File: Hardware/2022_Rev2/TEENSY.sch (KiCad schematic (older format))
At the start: 8 parts

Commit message: back to the teensy :alien:
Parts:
- removed U? (x8): TM4C129E_Launchpad, symbol MRDT_Shields:TM4C129E_Launchpad
- added U?: Teensy4.1_DEV-16771-MRDT_Shields, MODULE_DEV-16771, symbol 2022_Rev2-rescue:Teensy4.1_DEV-16771-MRDT_Shields
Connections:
- no-connect marks 0 -> 42
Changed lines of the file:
@@
 $Descr A4 11693 8268
 encoding utf-8
-Sheet 4 5
+Sheet 5 6
 Title ""
 Date ""
@@
 L power:GND #PWR?
 U 1 1 62120694
-P 6450 5600
-F 0 "#PWR?" H 6450 5350 50  0001 C CNN
-F 1 "GND" H 6455 5427 50  0000 C CNN
-F 2 "" H 6450 5600 50  0001 C CNN
-F 3 "" H 6450 5600 50  0001 C CNN
-	1    6450 5600
+P 6000 6100
+F 0 "#PWR?" H 6000 5850 50  0001 C CNN
+F 1 "GND" H 6005 5927 50  0000 C CNN
+F 2 "" H 6000 6100 50  0001 C CNN
+F 3 "" H 6000 6100 50  0001 C CNN
+	1    6000 6100
 	1    0    0    -1
 $EndComp
 Wire Wire Line
-	6250 5400 6450 5400
+	5800 5900 6000 5900
 Wire Wire Line
-	6450 5400 6450 5500
+	6000 5900 6000 6000
 Wire Wire Line
-	6250 5500 6450 5500
-Connection ~ 6450 5500
+	5800 6000 6000 6000
+Connection ~ 6000 6000
 Wire Wire Line
-	6450 5500 6450 5600
+	6000 6000 6000 6100
 $Comp
 L power:+3.3V #PWR?
 U 1 1 6220549B
-P 6550 1500
-F 0 "#PWR?" H 6550 1350 50  0001 C CNN
-F 1 "+3.3V" H 6565 1673 50  0000 C CNN
-F 2 "" H 6550 1500 50  0001 C CNN
-F 3 "" H 6550 1500 50  0001 C CNN
-	1    6550 1500
+P 6000 2100
+F 0 "#PWR?" H 6000 1950 50  0001 C CNN
+F 1 "+3.3V" H 6015 2273 50  0000 C CNN
+F 2 "" H 6000 2100 50  0001 C CNN
+F 3 "" H 6000 2100 50  0001 C CNN
+	1    6000 2100
 	1    0    0    -1
 $EndComp
 Wire Wire Line
-	6350 1700 6550 1700
+	5800 2300 6000 2300
 Wire Wire Line
-	6550 1700 6550 1500
-Text HLabel 3750 5150 0    50   Input ~ 0
+	6000 2300 6000 2100
+Text HLabel 4100 5400 0    50   Input ~ 0
 Current_Sense_BlackBox
-Text HLabel 3750 5050 0    50   Input ~ 0
+Text HLabel 4100 5300 0    50   Input ~ 0
 Current_Sense_Multimedia
-Text HLabel 3750 4950 0    50   Input ~ 0
+Text HLabel 4100 5200 0    50   Input ~ 0
 Current_Sense_Drive
-Text HLabel 3750 4850 0    50   Input ~ 0
+Text HLabel 4100 5100 0    50   Input ~ 0
 Current_Sense_Nav
-Text HLabel 3750 4750 0    50   Input ~ 0
+Text HLabel 4100 5000 0    50   Input ~ 0
 Current_Sense_Gimbal
-Text HLabel 3750 4650 0    50   Input ~ 0
+Text HLabel 4100 4900 0    50   Input ~ 0
 Current_Sense_Spare
 Wire Wire Line
-	3750 4650 3850 4650
+	4100 4900 4200 4900
 Wire Wire Line
-	3850 4750 3750 4750
+	4200 5000 4100 5000
 Wire Wire Line
-	3750 4850 3850 4850
+	4100 5100 4200 5100
 Wire Wire Line
-	3850 4950 3750 4950
+	4200 5200 4100 5200
 Wire Wire Line
-	3750 5050 3850 5050
+	4100 5300 4200 5300
 Wire Wire Line
-	3850 5150 3750 5150
-Text HLabel 3750 3050 0    50   Output ~ 0
+	4200 5400 4100 5400
+Text HLabel 4100 3300 0    50   Output ~ 0
 Driver_BlackBox
-Text HLabel 3750 3150 0    50   Output ~ 0
+Text HLabel 4100 3400 0    50   Output ~ 0
 Driver_Multimedia
-Text HLabel 3750 3250 0    50   Output ~ 0
+Text HLabel 4100 3500 0    50   Output ~ 0
 Driver_Drive
-Text HLabel 3750 3350 0    50   Output ~ 0
+Text HLabel 4100 3600 0    50   Output ~ 0
 Driver_Nav
-Text HLabel 3750 3450 0    50   Output ~ 0
+Text HLabel 4100 3700 0    50   Output ~ 0
 Driver_Gimbal
-Text HLabel 3750 3550 0    50   Output ~ 0
+Text HLabel 4100 3800 0    50   Output ~ 0
 Driver_Spare
 Wire Wire Line
-	3750 3050 3850 3050
+	4100 3300 4200 3300
 Wire Wire Line
-	3850 3150 3750 3150
+	4200 3400 4100 3400
 Wire Wire Line
-	3750 3250 3850 3250
+	4100 3500 4200 3500
 Wire Wire Line
-	3850 3350 3750 3350
+	4200 3600 4100 3600
 Wire Wire Line
-	3750 3450 3850 3450
+	4100 3700 4200 3700
 Wire Wire Line
-	3850 3550 3750 3550
+	4200 3800 4100 3800
 $Comp
-L MRDT_Shields:TM4C129E_Launchpad U?
-U 1 1 622A6302
-P 5000 3300
-F 0 "U?" H 5301 3898 60  0000 L CNN
-F 1 "TM4C129E_Launchpad" H 5301 3792 60  0000 L CNN
-F 2 "" H 5000 3300 60  0001 C CNN
-F 3 "" H 5000 3300 60  0001 C CNN
-	1    5000 3300
+L 2022_Rev2-rescue:Teensy4.1_DEV-16771-MRDT_Shields U?
+U 1 1 62325DE4
+P 5000 4100
+F 0 "U?" H 5000 6267 50  0000 C CNN
+F 1 "Teensy4.1_DEV-16771-MRDT_Shields" H 5000 6176 50  0000 C CNN
+F 2 "MODULE_DEV-16771" H 7100 3800 50  0001 L BNN
+F 3 "" H 5000 4100 50  0001 L BNN
+F 4 "Manufacturer recommendations" H 7100 3550 50  0001 L BNN "STANDARD"
+F 5 "4.07mm" H 7350 3350 50  0001 L BNN "MAXIMUM_PACKAGE_HEIGHT"
+F 6 "SparkFun Electronics" H 7300 3200 50  0001 L BNN "MANUFACTURER"
+F 7 "4.1" H 4700 1900 50  0001 L BNN "PARTREV"
+	1    5000 4100
 	1    0    0    -1
 $EndComp
-$Comp
-L MRDT_Shields:TM4C129E_Launchpad U?
-U 2 1 622A854E
-P 6700 3250
-F 0 "U?" H 6731 4527 60  0000 C CNN
-F 1 "TM4C129E_Launchpad" H 6731 4421 60  0000 C CNN
-F 2 "" H 6700 3250 60  0001 C CNN
-F 3 "" H 6700 3250 60  0001 C CNN
-	2    6700 3250
-	-1   0    0    -1
-$EndComp
-$Comp
-L MRDT_Shields:TM4C129E_Launchpad U?
-U 3 1 622AA5F6
-P 7950 3250
-F 0 "U?" H 8255 3848 60  0000 L CNN
-F 1 "TM4C129E_Launchpad" H 8255 3742 60  0000 L CNN
-F 2 "" H 7950 3250 60  0001 C CNN
-F 3 "" H 7950 3250 60  0001 C CNN
-	3    7950 3250
-	1    0    0    -1
-$EndComp
-$Comp
-L MRDT_Shields:TM4C129E_Launchpad U?
-U 4 1 622AE2B5
-P 9800 3200
-F 0 "U?" H 9831 4477 60  0000 C CNN
-F 1 "TM4C129E_Launchpad" H 9831 4371 60  0000 C CNN
-F 2 "" H 9800 3200 60  0001 C CNN
-F 3 "" H 9800 3200 60  0001 C CNN
-	4    9800 3200
-	-1   0    0    -1
-$EndComp
-$Comp
-L MRDT_Shields:TM4C129E_Launchpad U?
-U 5 1 622B0F3D
-P 5000 4650
-F 0 "U?" H 5301 5248 60  0000 L CNN
-F 1 "TM4C129E_Launchpad" H 5301 5142 60  0000 L CNN
-F 2 "" H 5000 4650 60  0001 C CNN
-F 3 "" H 5000 4650 60  0001 C CNN
-	5    5000 4650
-	1    0    0    -1
-$EndComp
-$Comp
-L MRDT_Shields:TM4C129E_Launchpad U?
-U 6 1 622B4CAE
-P 6700 4700
-F 0 "U?" H 6731 5977 60  0000 C CNN
-F 1 "TM4C129E_Launchpad" H 6731 5871 60  0000 C CNN
-F 2 "" H 6700 4700 60  0001 C CNN
-F 3 "" H 6700 4700 60  0001 C CNN
-	6    6700 4700
-	-1   0    0    -1
-$EndComp
-$Comp
-L MRDT_Shields:TM4C129E_Launchpad U?
-U 7 1 622B6EBF
-P 7950 4750
-F 0 "U?" H 8255 5348 60  0000 L CNN
-F 1 "TM4C129E_Launchpad" H 8255 5242 60  0000 L CNN
-F 2 "" H 7950 4750 60  0001 C CNN
-F 3 "" H 7950 4750 60  0001 C CNN
-	7    7950 4750
-	1    0    0    -1
-$EndComp
-$Comp
-L MRDT_Shields:TM4C129E_Launchpad U?
-U 8 1 622B9460
-P 9750 4750
-F 0 "U?" H 9781 6027 60  0000 C CNN
-F 1 "TM4C129E_Launchpad" H 9781 5921 60  0000 C CNN
-F 2 "" H 9750 4750 60  0001 C CNN
-F 3 "" H 9750 4750 60  0001 C CNN
-	8    9750 4750
-	-1   0    0    -1
-$EndComp
+NoConn ~ 4200 2700
+NoConn ~ 4200 2800
+NoConn ~ 4200 3000
+NoConn ~ 4200 3100
+NoConn ~ 4200 3900
+NoConn ~ 4200 4000
+NoConn ~ 4200 4100
+NoConn ~ 4200 4200
+NoConn ~ 4200 4400
+NoConn ~ 4200 4500
+NoConn ~ 4200 4600
+NoConn ~ 4200 4700
+NoConn ~ 4200 5500
+NoConn ~ 4200 5600
+NoConn ~ 4200 5700
+NoConn ~ 5800 5700
+NoConn ~ 5800 5600
+NoConn ~ 5800 5500
+NoConn ~ 5800 5400
+NoConn ~ 5800 5300
+NoConn ~ 5800 5200
+NoConn ~ 5800 5100
+NoConn ~ 5800 5000
+NoConn ~ 5800 4900
+NoConn ~ 5800 4600
+NoConn ~ 5800 4500
+NoConn ~ 5800 4300
+NoConn ~ 5800 4200
+NoConn ~ 5800 4100
+NoConn ~ 5800 3900
+NoConn ~ 5800 3800
+NoConn ~ 5800 3700
+NoConn ~ 5800 3600
+NoConn ~ 5800 3400
+NoConn ~ 5800 3300
+NoConn ~ 5800 3100
+NoConn ~ 5800 3000
+NoConn ~ 5800 2900
+NoConn ~ 5800 2800
+NoConn ~ 5800 2700
+NoConn ~ 5800 2500
+NoConn ~ 5800 2400
 $EndSCHEMATC

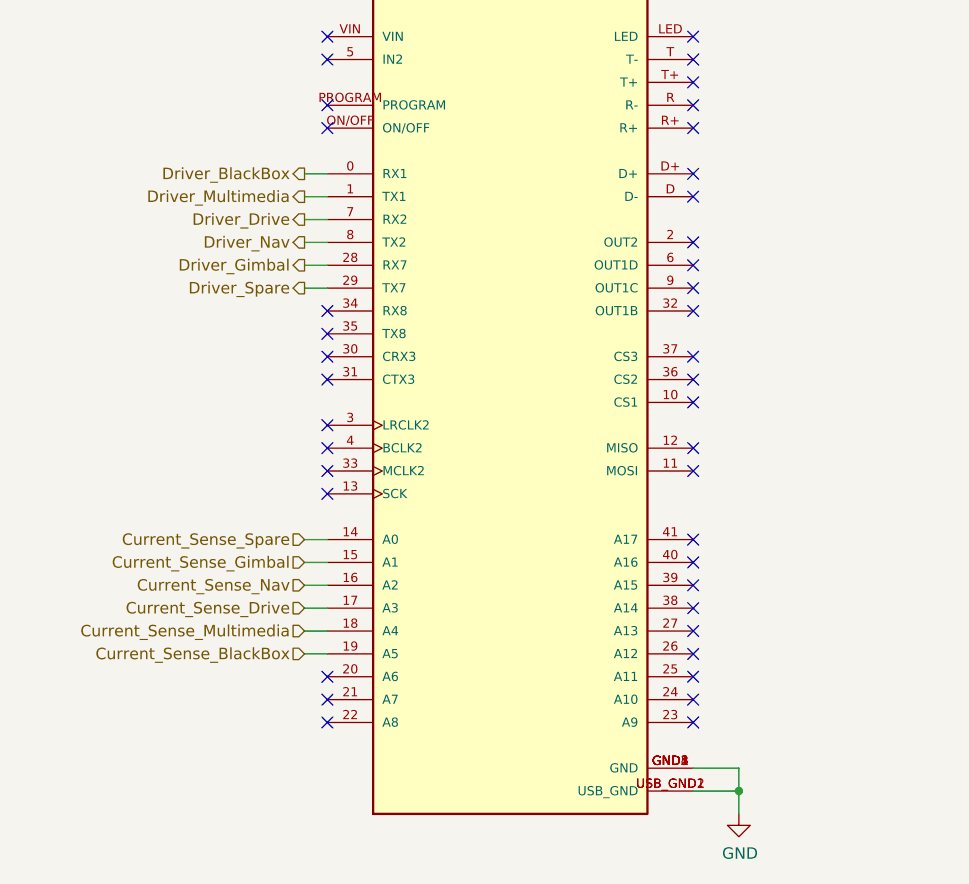
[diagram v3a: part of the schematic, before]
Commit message: teensy pins are done (I think)
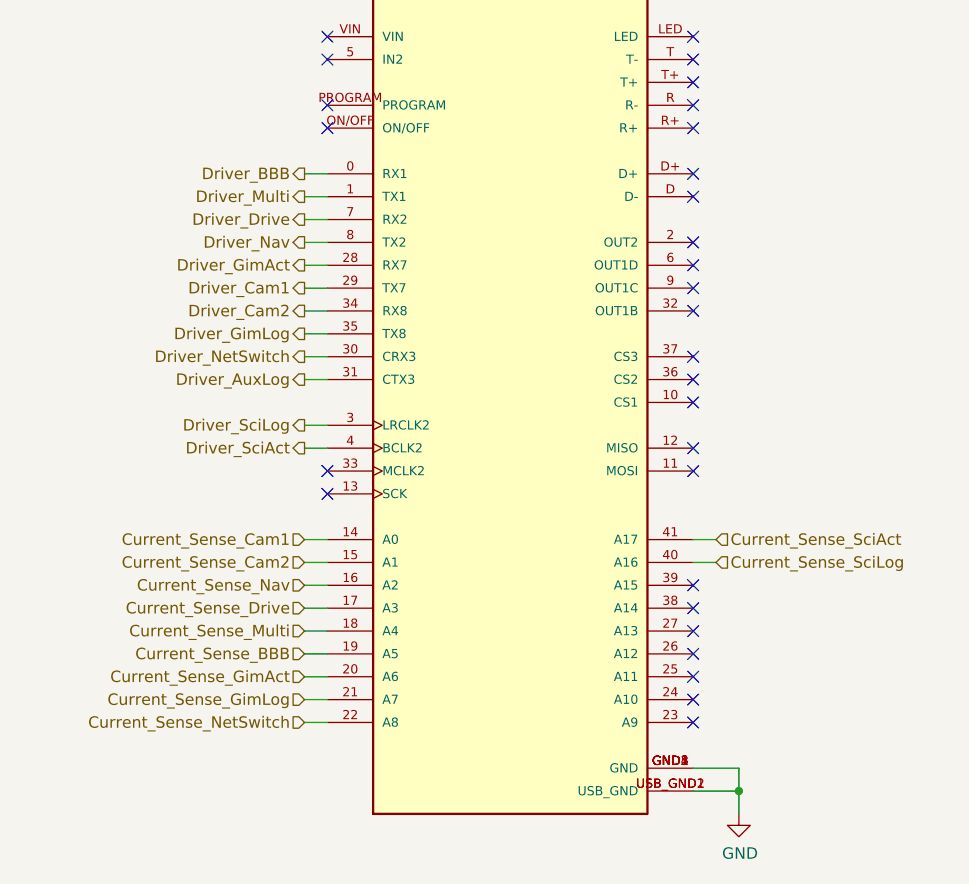
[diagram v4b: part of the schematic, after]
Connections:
- net Current_Sense_GimAct: now reaches U?.20 (A6)
- net Current_Sense_GimLog: now reaches U?.21 (A7)
- net Current_Sense_NetSwitch: now reaches U?.22 (A8)
- net Driver_SciLog: now reaches U?.3 (LRCLK2)
- net Driver_NetSwitch: now reaches U?.30 (CRX3)
- net Driver_AuxLog: now reaches U?.31 (CTX3)
- net Driver_Cam2: now reaches U?.34 (RX8)
- net Driver_GimLog: now reaches U?.35 (TX8)
- net Driver_SciAct: now reaches U?.4 (BCLK2)
- net Current_Sense_SciLog: now reaches U?.40 (A16)
- net Current_Sense_SciAct: now reaches U?.41 (A17)
- net Current_Sense_BlackBox renamed Current_Sense_BBB
- net Current_Sense_Gimbal renamed Current_Sense_Cam2
- net Current_Sense_Multimedia renamed Current_Sense_Multi
- net Current_Sense_Spare renamed Current_Sense_Cam1
- net Driver_BlackBox renamed Driver_BBB
- net Driver_Gimbal renamed Driver_GimAct
- net Driver_Multimedia renamed Driver_Multi
- net Driver_Spare renamed Driver_Cam1
- no-connect marks 42 -> 31
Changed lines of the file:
@@
 $Descr A4 11693 8268
 encoding utf-8
-Sheet 5 6
+Sheet 4 5
 Title ""
 Date ""
@@
 	6000 2300 6000 2100
 Text HLabel 4100 5400 0    50   Input ~ 0
-Current_Sense_BlackBox
+Current_Sense_BBB
 Text HLabel 4100 5300 0    50   Input ~ 0
-Current_Sense_Multimedia
+Current_Sense_Multi
 Text HLabel 4100 5200 0    50   Input ~ 0
 Current_Sense_Drive
@@
 Current_Sense_Nav
 Text HLabel 4100 5000 0    50   Input ~ 0
-Current_Sense_Gimbal
+Current_Sense_Cam2
 Text HLabel 4100 4900 0    50   Input ~ 0
-Current_Sense_Spare
+Current_Sense_Cam1
 Wire Wire Line
 	4100 4900 4200 4900
@@
 	4200 5400 4100 5400
 Text HLabel 4100 3300 0    50   Output ~ 0
-Driver_BlackBox
+Driver_BBB
 Text HLabel 4100 3400 0    50   Output ~ 0
-Driver_Multimedia
+Driver_Multi
 Text HLabel 4100 3500 0    50   Output ~ 0
 Driver_Drive
@@
 Driver_Nav
 Text HLabel 4100 3700 0    50   Output ~ 0
-Driver_Gimbal
+Driver_GimAct
 Text HLabel 4100 3800 0    50   Output ~ 0
-Driver_Spare
+Driver_Cam1
 Wire Wire Line
 	4100 3300 4200 3300
@@
 Wire Wire Line
 	4200 3800 4100 3800
-$Comp
-L 2022_Rev2-rescue:Teensy4.1_DEV-16771-MRDT_Shields U?
-U 1 1 62325DE4
-P 5000 4100
-F 0 "U?" H 5000 6267 50  0000 C CNN
-F 1 "Teensy4.1_DEV-16771-MRDT_Shields" H 5000 6176 50  0000 C CNN
-F 2 "MODULE_DEV-16771" H 7100 3800 50  0001 L BNN
-F 3 "" H 5000 4100 50  0001 L BNN
-F 4 "Manufacturer recommendations" H 7100 3550 50  0001 L BNN "STANDARD"
-F 5 "4.07mm" H 7350 3350 50  0001 L BNN "MAXIMUM_PACKAGE_HEIGHT"
-F 6 "SparkFun Electronics" H 7300 3200 50  0001 L BNN "MANUFACTURER"
-F 7 "4.1" H 4700 1900 50  0001 L BNN "PARTREV"
-	1    5000 4100
-	1    0    0    -1
-$EndComp
 NoConn ~ 4200 2700
 NoConn ~ 4200 2800
 NoConn ~ 4200 3000
 NoConn ~ 4200 3100
-NoConn ~ 4200 3900
-NoConn ~ 4200 4000
-NoConn ~ 4200 4100
-NoConn ~ 4200 4200
-NoConn ~ 4200 4400
-NoConn ~ 4200 4500
-NoConn ~ 4200 4600
-NoConn ~ 4200 4700
-NoConn ~ 4200 5500
-NoConn ~ 4200 5600
-NoConn ~ 4200 5700
 NoConn ~ 5800 5700
 NoConn ~ 5800 5600
@@
 NoConn ~ 5800 5200
 NoConn ~ 5800 5100
-NoConn ~ 5800 5000
-NoConn ~ 5800 4900
 NoConn ~ 5800 4600
 NoConn ~ 5800 4500
@@
 NoConn ~ 5800 2500
 NoConn ~ 5800 2400
+Text HLabel 4100 3900 0    50   Output ~ 0
+Driver_Cam2
+Wire Wire Line
+	4200 3900 4100 3900
+Text HLabel 4100 5500 0    50   Input ~ 0
+Current_Sense_GimAct
+Wire Wire Line
+	4100 5500 4200 5500
+$Comp
+L 2022_Rev2-rescue:Teensy4.1_DEV-16771-MRDT_Shields U?
+U 1 1 62325DE4
+P 5000 4100
+F 0 "U?" H 5000 6267 50  0000 C CNN
+F 1 "Teensy4.1_DEV-16771-MRDT_Shields" H 5000 6176 50  0000 C CNN
+F 2 "MODULE_DEV-16771" H 7100 3800 50  0001 L BNN
+F 3 "" H 5000 4100 50  0001 L BNN
+F 4 "Manufacturer recommendations" H 7100 3550 50  0001 L BNN "STANDARD"
+F 5 "4.07mm" H 7350 3350 50  0001 L BNN "MAXIMUM_PACKAGE_HEIGHT"
+F 6 "SparkFun Electronics" H 7300 3200 50  0001 L BNN "MANUFACTURER"
+F 7 "4.1" H 4700 1900 50  0001 L BNN "PARTREV"
+	1    5000 4100
+	1    0    0    -1
+$EndComp
+Text HLabel 4100 4000 0    50   Output ~ 0
+Driver_GimLog
+Wire Wire Line
+	4100 4000 4200 4000
+Text HLabel 4100 4100 0    50   Output ~ 0
+Driver_NetSwitch
+Wire Wire Line
+	4100 4100 4200 4100
+Text HLabel 4100 4200 0    50   Output ~ 0
+Driver_AuxLog
+Wire Wire Line
+	4100 4200 4200 4200
+Text HLabel 4100 4400 0    50   Output ~ 0
+Driver_SciLog
+Wire Wire Line
+	4100 4400 4200 4400
+Text HLabel 4100 4500 0    50   Output ~ 0
+Driver_SciAct
+Wire Wire Line
+	4100 4500 4200 4500
+NoConn ~ 4200 4600
+NoConn ~ 4200 4700
+Text HLabel 4100 5600 0    50   Input ~ 0
+Current_Sense_GimLog
+Wire Wire Line
+	4100 5600 4200 5600
+Text HLabel 4100 5700 0    50   Input ~ 0
+Current_Sense_NetSwitch
+Wire Wire Line
+	4100 5700 4200 5700
+Text HLabel 5900 4900 2    50   Input ~ 0
+Current_Sense_SciAct
+Wire Wire Line
+	5900 4900 5800 4900
+Text HLabel 5900 5000 2    50   Input ~ 0
+Current_Sense_SciLog
+Wire Wire Line
+	5900 5000 5800 5000
 $EndSCHEMATC

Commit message: andersons done
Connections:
- net Current_Sense_AuxLog: now reaches U?.39 (A15)
- no-connect marks 31 -> 30
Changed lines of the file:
@@
 $Descr A4 11693 8268
 encoding utf-8
-Sheet 4 5
+Sheet 5 5
 Title ""
 Date ""
@@
 NoConn ~ 5800 5300
 NoConn ~ 5800 5200
-NoConn ~ 5800 5100
 NoConn ~ 5800 4600
 NoConn ~ 5800 4500
@@
 Wire Wire Line
 	5900 5000 5800 5000
+Text HLabel 5900 5100 2    50   Input ~ 0
+Current_Sense_AuxLog
+Wire Wire Line
+	5900 5100 5800 5100
 $EndSCHEMATC
